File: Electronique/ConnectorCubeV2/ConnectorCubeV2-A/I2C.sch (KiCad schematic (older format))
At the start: 21 parts, among them J201 Conn_01x04, J202 Conn_01x04, J203 Conn_01x04, U201 PCA9306, U202 PCA9306, U203 PCA9306

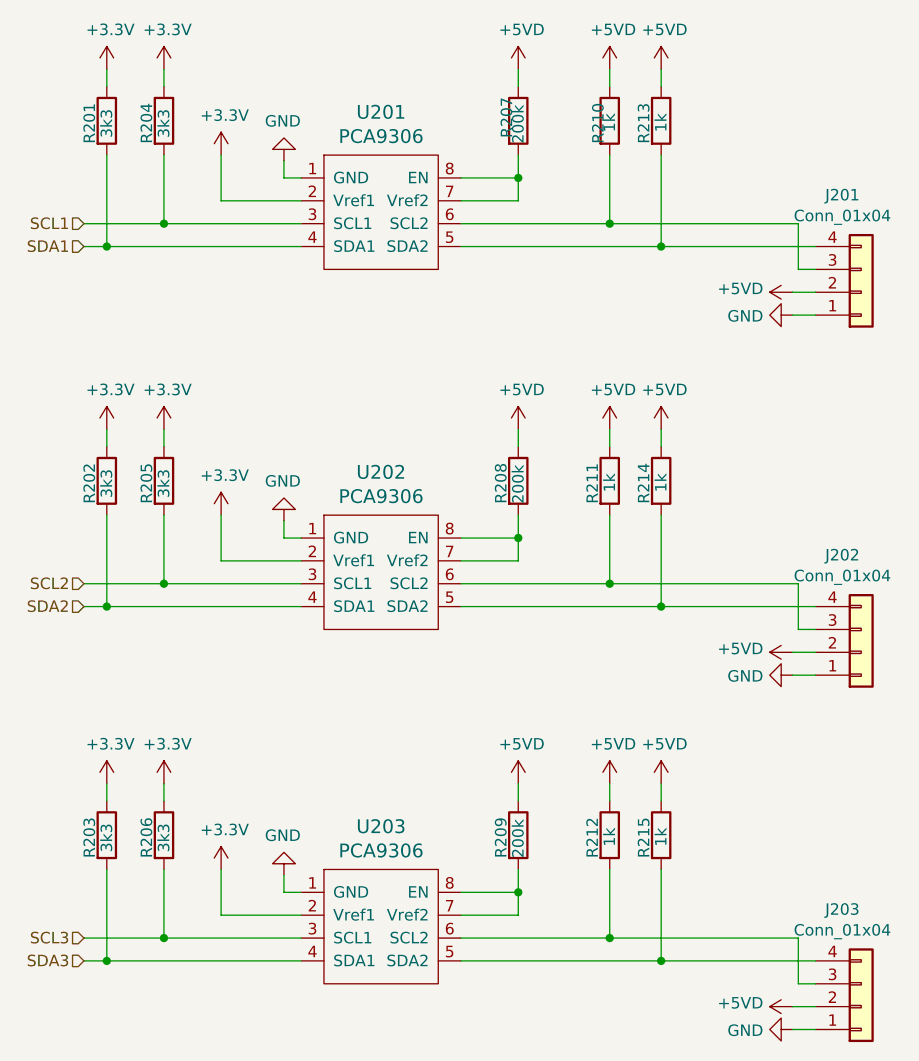
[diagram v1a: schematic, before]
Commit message: V206 TM1638 7Segments Begin
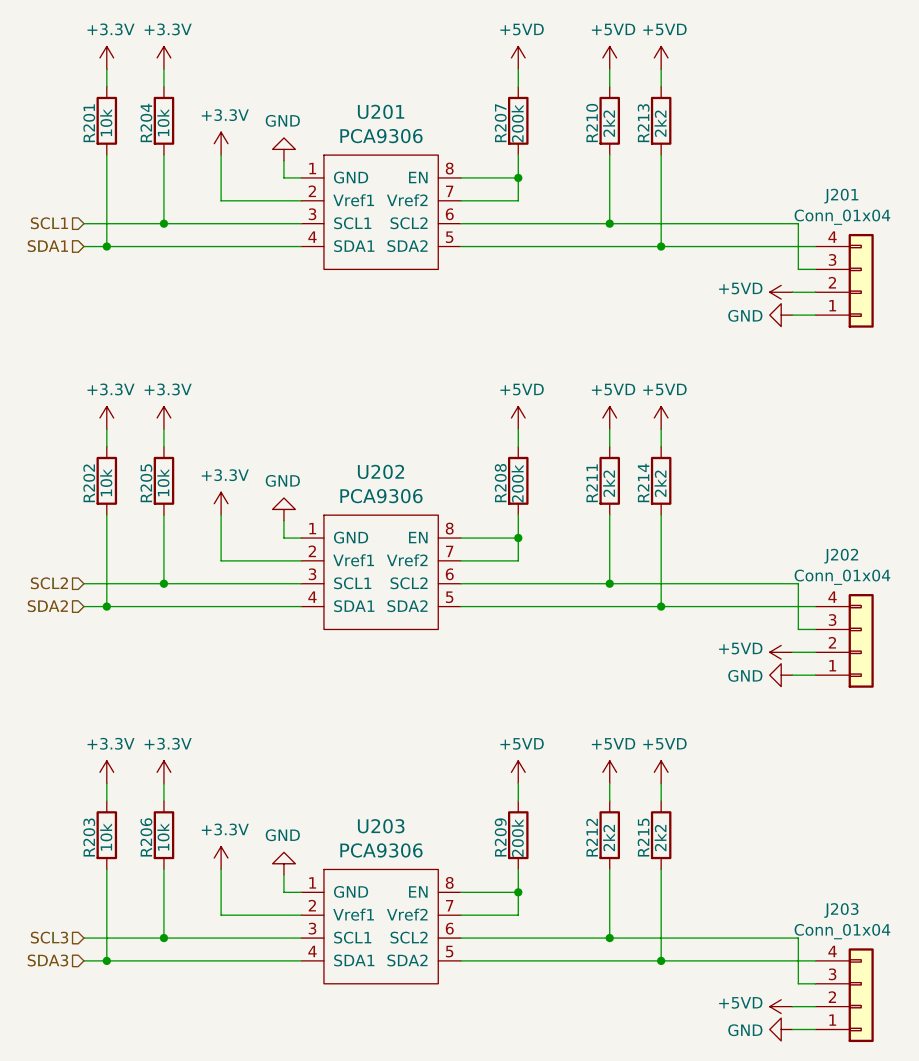
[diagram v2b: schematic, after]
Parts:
- R201, R202, R203, R204, R205, R206: value 3k3 -> 10k
- R210, R211, R212, R213, R214, R215: value 1k -> 2k2
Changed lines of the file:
@@
 AR Path="/61AE59BE/61AEED6A" Ref="R204"  Part="1"
 F 0 "R204" V 4800 2000 50  0000 L CNN
-F 1 "3k3" V 4875 2025 50  0000 L CNN
+F 1 "10k" V 4875 2025 50  0000 L CNN
 F 2 "Resistor_SMD:R_0603_1608Metric" V 4805 2100 50  0001 C CNN
 F 3 "~" H 4875 2100 50  0001 C CNN
@@
 AR Path="/61AE546C/61AEED70" Ref="R?"  Part="1"
 AR Path="/61AE59BE/61AEED70" Ref="R207"  Part="1"
-F 0 "R207" V 6375 2025 50  0000 L CNN
+F 0 "R207" V 6350 2000 50  0000 L CNN
 F 1 "200k" V 6425 2000 50  0000 L CNN
 F 2 "Resistor_SMD:R_0603_1608Metric" V 6355 2100 50  0001 C CNN
@@
 AR Path="/61AE546C/61AEED76" Ref="R?"  Part="1"
 AR Path="/61AE59BE/61AEED76" Ref="R210"  Part="1"
-F 0 "R210" V 6775 2000 50  0000 L CNN
-F 1 "1k" V 6825 2050 50  0000 L CNN
+F 0 "R210" V 6750 2000 50  0000 L CNN
+F 1 "2k2" V 6825 2025 50  0000 L CNN
 F 2 "Resistor_SMD:R_0603_1608Metric" V 6755 2100 50  0001 C CNN
 F 3 "~" H 6825 2100 50  0001 C CNN
@@
 AR Path="/61AE59BE/61AEED9E" Ref="R201"  Part="1"
 F 0 "R201" V 4550 2000 50  0000 L CNN
-F 1 "3k3" V 4625 2025 50  0000 L CNN
+F 1 "10k" V 4625 2025 50  0000 L CNN
 F 2 "Resistor_SMD:R_0603_1608Metric" V 4555 2100 50  0001 C CNN
 F 3 "~" H 4625 2100 50  0001 C CNN
@@
 AR Path="/61AE59BE/61AEEDA4" Ref="R213"  Part="1"
 F 0 "R213" V 6975 2000 50  0000 L CNN
-F 1 "1k" V 7050 2050 50  0000 L CNN
+F 1 "2k2" V 7050 2025 50  0000 L CNN
 F 2 "Resistor_SMD:R_0603_1608Metric" V 6980 2100 50  0001 C CNN
 F 3 "~" H 7050 2100 50  0001 C CNN
@@
 AR Path="/61AE59BE/61AF09E3" Ref="R205"  Part="1"
 F 0 "R205" V 4800 3575 50  0000 L CNN
-F 1 "3k3" V 4875 3600 50  0000 L CNN
+F 1 "10k" V 4875 3600 50  0000 L CNN
 F 2 "Resistor_SMD:R_0603_1608Metric" V 4805 3675 50  0001 C CNN
 F 3 "~" H 4875 3675 50  0001 C CNN
@@
 AR Path="/61AE59BE/61AF09F7" Ref="R211"  Part="1"
 F 0 "R211" V 6750 3575 50  0000 L CNN
-F 1 "1k" V 6825 3625 50  0000 L CNN
+F 1 "2k2" V 6825 3600 50  0000 L CNN
 F 2 "Resistor_SMD:R_0603_1608Metric" V 6755 3675 50  0001 C CNN
 F 3 "~" H 6825 3675 50  0001 C CNN
@@
 AR Path="/61AE59BE/61AF0A33" Ref="R202"  Part="1"
 F 0 "R202" V 4550 3575 50  0000 L CNN
-F 1 "3k3" V 4625 3600 50  0000 L CNN
+F 1 "10k" V 4625 3600 50  0000 L CNN
 F 2 "Resistor_SMD:R_0603_1608Metric" V 4555 3675 50  0001 C CNN
 F 3 "~" H 4625 3675 50  0001 C CNN
@@
 AR Path="/61AE59BE/61AF0A3D" Ref="R214"  Part="1"
 F 0 "R214" V 6975 3575 50  0000 L CNN
-F 1 "1k" V 7050 3625 50  0000 L CNN
+F 1 "2k2" V 7050 3600 50  0000 L CNN
 F 2 "Resistor_SMD:R_0603_1608Metric" V 6980 3675 50  0001 C CNN
 F 3 "~" H 7050 3675 50  0001 C CNN
@@
 AR Path="/61AE59BE/61AF9AB3" Ref="R206"  Part="1"
 F 0 "R206" V 4800 5125 50  0000 L CNN
-F 1 "3k3" V 4875 5150 50  0000 L CNN
+F 1 "10k" V 4875 5150 50  0000 L CNN
 F 2 "Resistor_SMD:R_0603_1608Metric" V 4805 5225 50  0001 C CNN
 F 3 "~" H 4875 5225 50  0001 C CNN
@@
 AR Path="/61AE59BE/61AF9AC7" Ref="R212"  Part="1"
 F 0 "R212" V 6750 5125 50  0000 L CNN
-F 1 "1k" V 6825 5175 50  0000 L CNN
+F 1 "2k2" V 6825 5150 50  0000 L CNN
 F 2 "Resistor_SMD:R_0603_1608Metric" V 6755 5225 50  0001 C CNN
 F 3 "~" H 6825 5225 50  0001 C CNN
@@
 AR Path="/61AE59BE/61AF9B03" Ref="R203"  Part="1"
 F 0 "R203" V 4550 5125 50  0000 L CNN
-F 1 "3k3" V 4625 5150 50  0000 L CNN
+F 1 "10k" V 4625 5150 50  0000 L CNN
 F 2 "Resistor_SMD:R_0603_1608Metric" V 4555 5225 50  0001 C CNN
 F 3 "~" H 4625 5225 50  0001 C CNN
@@
 AR Path="/61AE59BE/61AF9B0D" Ref="R215"  Part="1"
 F 0 "R215" V 6975 5125 50  0000 L CNN
-F 1 "1k" V 7050 5175 50  0000 L CNN
+F 1 "2k2" V 7050 5150 50  0000 L CNN
 F 2 "Resistor_SMD:R_0603_1608Metric" V 6980 5225 50  0001 C CNN
 F 3 "~" H 7050 5225 50  0001 C CNN
